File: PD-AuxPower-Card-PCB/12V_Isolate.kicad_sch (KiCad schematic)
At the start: 32 parts, among them J4 2.54mm terminal, Q1 FDMC86520L, T1 ER 9.5, U12 TL431DBZ, U7 LTV-217

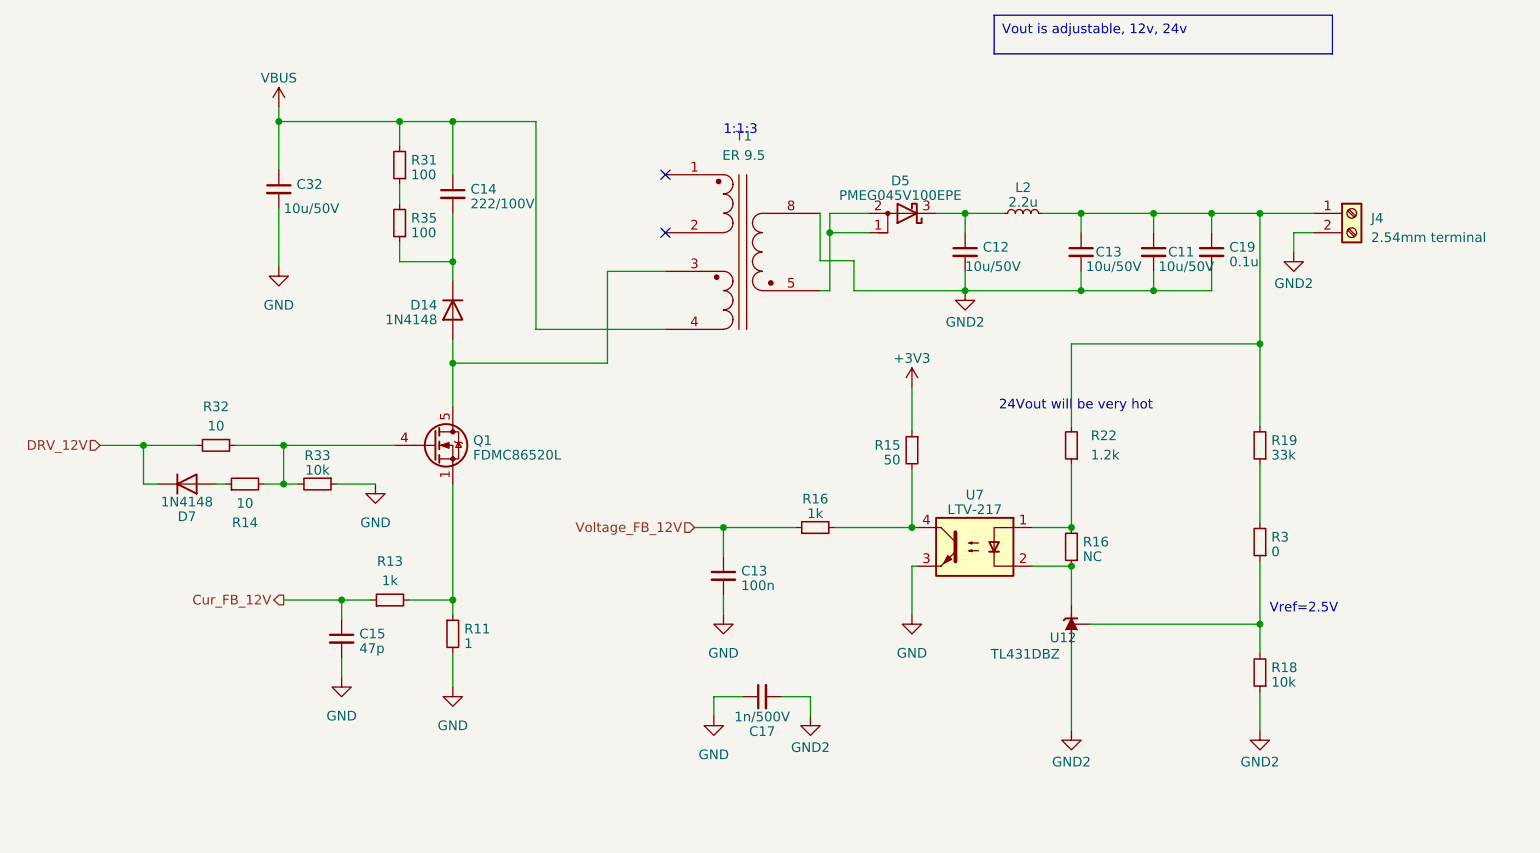
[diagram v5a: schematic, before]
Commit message: FEAT: Set I2C mode to standard mode(100kHz), change FUSB302B driver header file definition, trimming output voltage of 3.3/5V channel and 12/24V channel by optocoupler current reduce to 1mA. Add reserved PD protocol header and source file named pd_sink.h/.c. Add FUSB302B initial sequence and read/write driver. PCB: remove some unused protection diode, modify resistance.
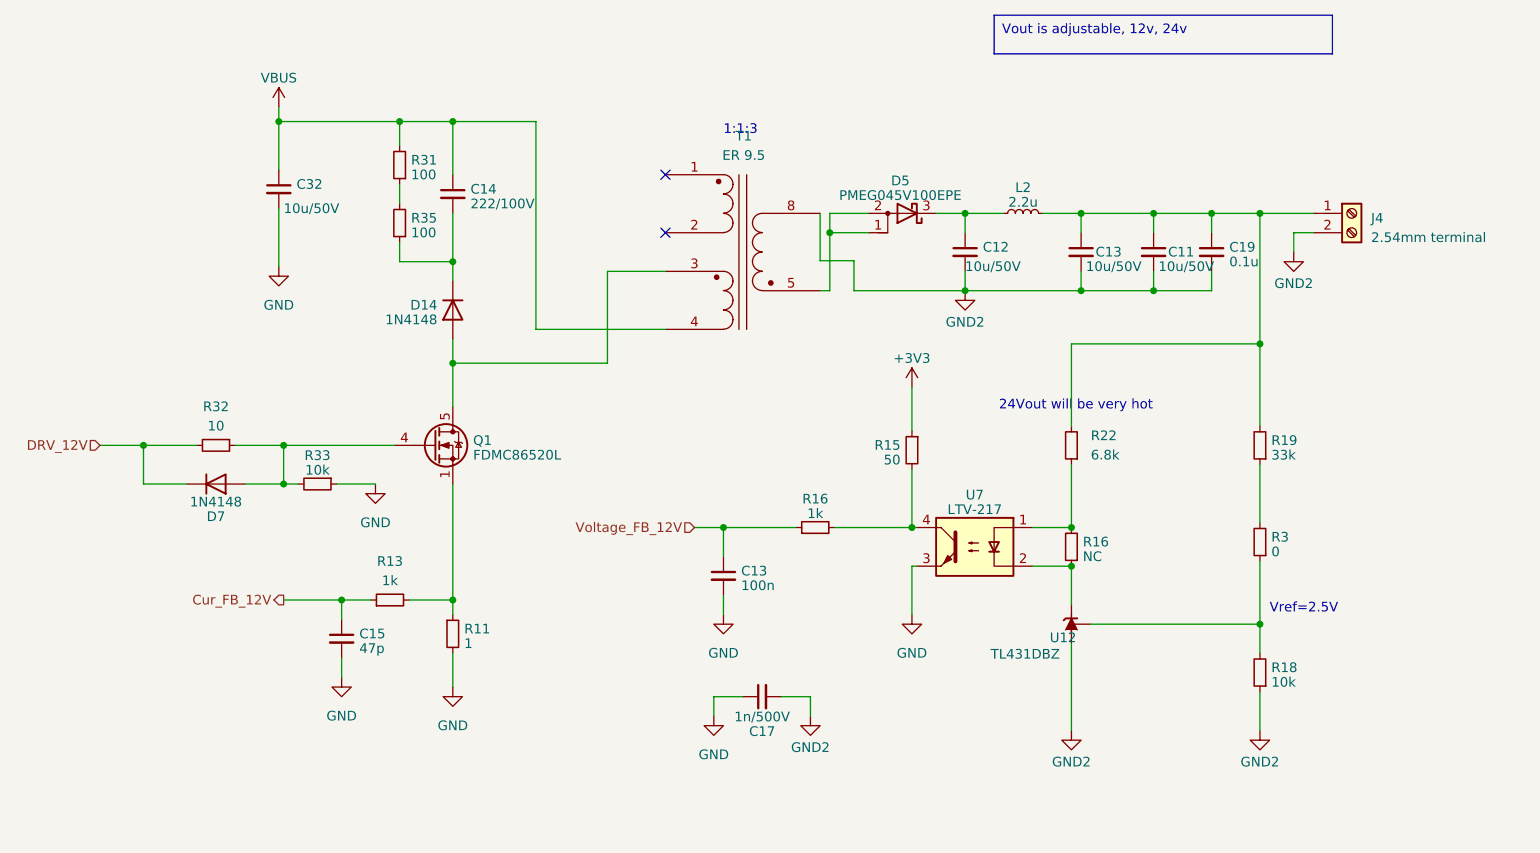
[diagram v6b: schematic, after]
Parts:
- removed R14: 10, Resistor_SMD:R_0402_1005Metric, symbol Device:R_Small
- R22: value 1.2k -> 6.8k
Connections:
- net at Q1.4 (G), R32.1, R33.2: now also D7.2 (A)
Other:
- moved on the sheet: D7
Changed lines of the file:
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@@
     (stroke (width 0) (type default))
   )
-  (wire (pts (xy 93.345 96.52) (xy 95.885 96.52))
+  (wire (pts (xy 90.805 96.52) (xy 95.885 96.52))
     (stroke (width 0) (type default))
   )
@@
     (stroke (width 0) (type default))
   )
-  (wire (pts (xy 77.47 96.52) (xy 79.375 96.52))
+  (wire (pts (xy 77.47 96.52) (xy 83.185 96.52))
     (stroke (width 0) (type default))
   )
@@
   )
   (wire (pts (xy 111.125 48.895) (xy 118.11 48.895))
-    (stroke (width 0) (type default))
-  )
-  (wire (pts (xy 86.995 96.52) (xy 88.265 96.52))
     (stroke (width 0) (type default))
   )
@@
     )
   )
-  (symbol (lib_id "Diode:1N4148") (at 83.185 96.52 0) (mirror x) (unit 1)
+  (symbol (lib_id "Diode:1N4148") (at 86.995 96.52 0) (mirror x) (unit 1)
     (in_bom yes) (on_board yes) (dnp no)
-    (property "Reference" "D7" (at 83.185 100.7999 0)
-      (effects (font (size 1.27 1.27)))
-    )
-    (property "Value" "1N4148" (at 83.185 98.8789 0)
-      (effects (font (size 1.27 1.27)))
-    )
-    (property "Footprint" "Diode_SMD:D_SOD-523" (at 83.185 96.52 0)
-      (effects (font (size 1.27 1.27)) hide)
-    )
-    (property "Datasheet" "https://assets.nexperia.com/documents/data-sheet/1N4148_1N4448.pdf" (at 83.185 96.52 0)
-      (effects (font (size 1.27 1.27)) hide)
-    )
-    (property "Sim.Device" "D" (at 83.185 96.52 0)
-      (effects (font (size 1.27 1.27)) hide)
-    )
-    (property "Sim.Pins" "1=K 2=A" (at 83.185 96.52 0)
+    (property "Reference" "D7" (at 86.995 100.7999 0)
+      (effects (font (size 1.27 1.27)))
+    )
+    (property "Value" "1N4148" (at 86.995 98.8789 0)
+      (effects (font (size 1.27 1.27)))
+    )
+    (property "Footprint" "Diode_SMD:D_SOD-523" (at 86.995 96.52 0)
+      (effects (font (size 1.27 1.27)) hide)
+    )
+    (property "Datasheet" "https://assets.nexperia.com/documents/data-sheet/1N4148_1N4448.pdf" (at 86.995 96.52 0)
+      (effects (font (size 1.27 1.27)) hide)
+    )
+    (property "Sim.Device" "D" (at 86.995 96.52 0)
+      (effects (font (size 1.27 1.27)) hide)
+    )
+    (property "Sim.Pins" "1=K 2=A" (at 86.995 96.52 0)
       (effects (font (size 1.27 1.27)) hide)
     )
@@
       (effects (font (size 1.27 1.27)) (justify right))
     )
-    (property "Value" "1.2k" (at 201.93 92.71 0)
+    (property "Value" "6.8k" (at 201.93 92.71 0)
       (effects (font (size 1.27 1.27)) (justify right))
     )
@@
         )
       )
-    )
-  )
-  (symbol (lib_id "Device:R_Small") (at 90.805 96.52 90) (unit 1)
-    (in_bom yes) (on_board yes) (dnp no)
-    (property "Reference" "R14" (at 90.805 101.6 90)
-      (effects (font (size 1.27 1.27)))
-    )
-    (property "Value" "10" (at 90.805 99.06 90)
-      (effects (font (size 1.27 1.27)))
-    )
-    (property "Footprint" "Resistor_SMD:R_0402_1005Metric" (at 90.805 96.52 0)
-      (effects (font (size 1.27 1.27)) hide)
-    )
-    (property "Datasheet" "~" (at 90.805 96.52 0)
-      (effects (font (size 1.27 1.27)) hide)
-    )
-    (pin "1")
-    (pin "2")
-    (instances
-      (project "PD-AuxPower-Card"
-        (path "/48c5bc14-ccc3-44de-b526-838e3d53c0ee/40f113c1-6183-4863-b2ec-a4ca33698158"
-          (reference "R14") (unit 1)
-        )
-        (path "/48c5bc14-ccc3-44de-b526-838e3d53c0ee/9a44a331-fce1-4dee-b5a9-6d547d8c4b08"
-          (reference "R47") (unit 1)
-        )
-      )

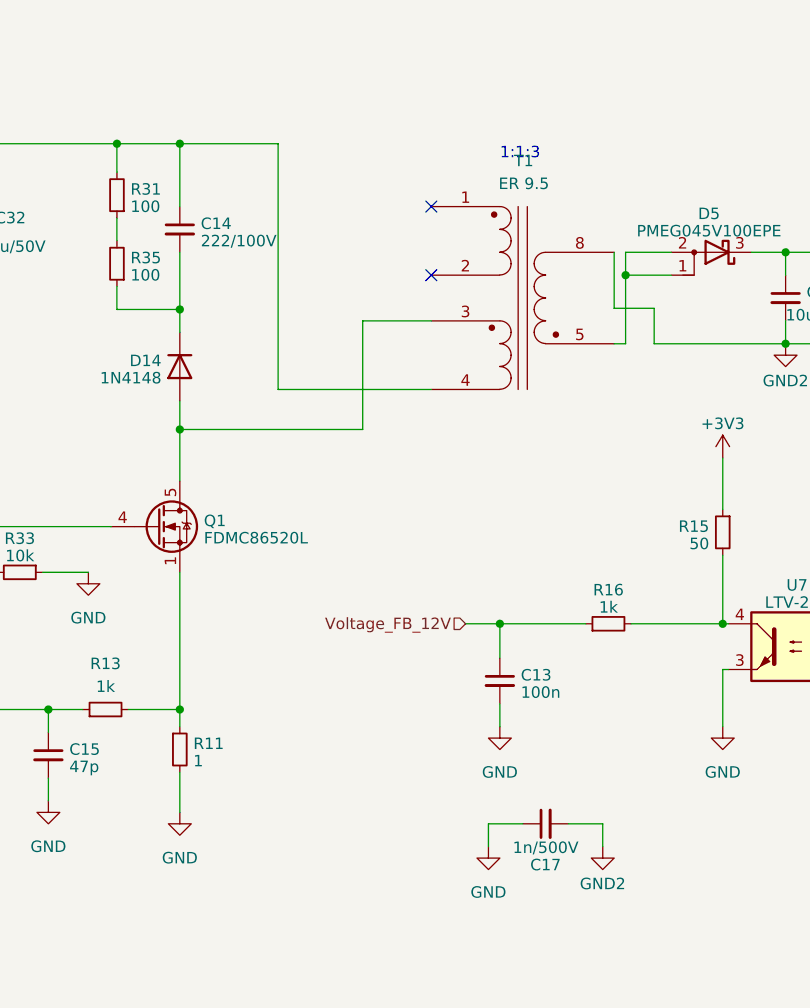
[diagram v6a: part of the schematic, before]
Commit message: FEAT: Revolution PCB to ver 1.0. Change COMP1+ to 3v3 current sense, COMP2+ to 12V current sense and 12V LED to GPIO7 output. Modify PCB layout.
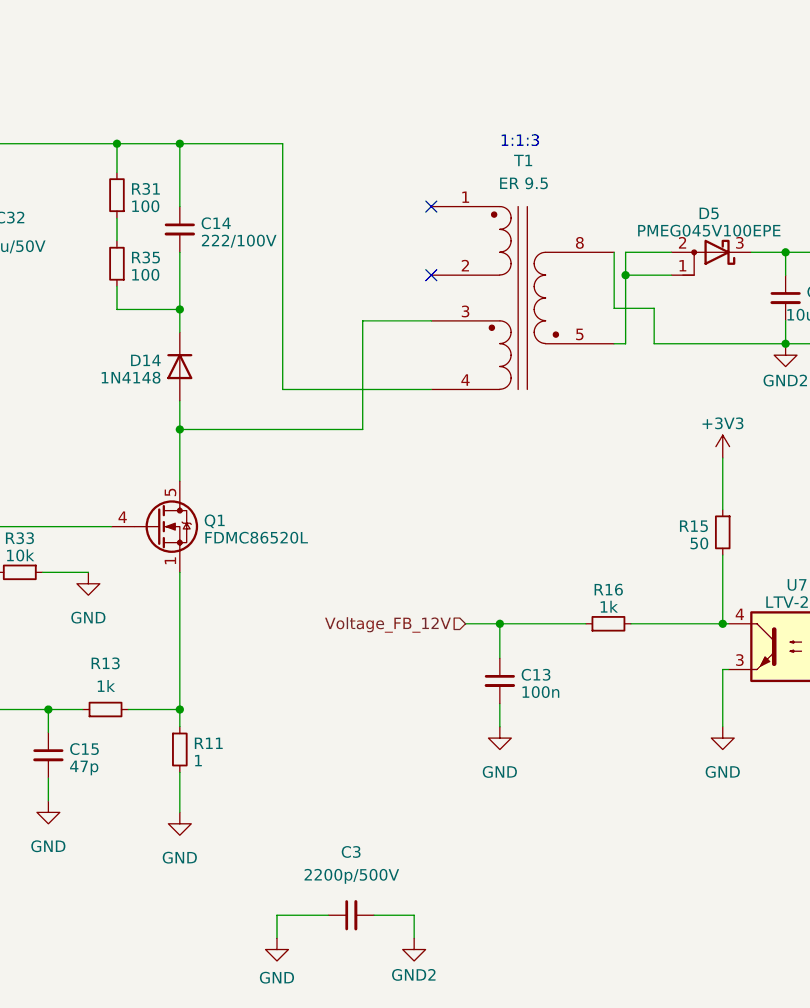
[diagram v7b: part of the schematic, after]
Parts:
- removed C17: 1n/500V, Capacitor_SMD:C_1210_3225Metric, symbol Device:C_Small
- added C3: 2200p/500V, Capacitor_SMD:C_1206_3216Metric, symbol Device:C_Small
- T1: footprint User:Transformer_ER9.5_11.6mmx8.2mm -> Johnson's:Transformer_ER9.5_11.6mmx8.2mm
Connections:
- net GND: now also C3.1
- net GND2: now also C3.2
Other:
- company: (none) -> Habonroof Playground
- title: (none) -> 12/24V Flyback converter
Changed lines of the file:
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@@
 (kicad_sch (version 20230121) (generator eeschema)
   (paper "A4")
+  (title_block
+    (title "12/24V Flyback converter")
+    (date "2023-11-26")
+    (rev "Rev 1.0")
+    (company "Habonroof Playground")
+  )
   (junction (at 95.885 91.44) (diameter 0) (color 0 0 0 0)
   )
@@
     (stroke (width 0) (type default))
   )
-  (wire (pts (xy 156.21 124.46) (xy 152.4 124.46))
-    (stroke (width 0) (type default))
-  )
   (wire (pts (xy 200.66 68.58) (xy 200.66 71.12))
     (stroke (width 0) (type default))
@@
     (stroke (width 0) (type default))
   )
-  (wire (pts (xy 146.05 76.2) (xy 129.032 76.2))
+  (wire (pts (xy 146.05 76.2) (xy 129.54 76.2))
     (stroke (width 0) (type default))
   )
@@
     (stroke (width 0) (type default))
   )
+  (wire (pts (xy 144.145 134.62) (xy 144.145 137.16))
+    (stroke (width 0) (type default))
+  )
   (wire (pts (xy 168.275 102.235) (xy 178.435 102.235))
     (stroke (width 0) (type default))
@@
     (stroke (width 0) (type default))
   )
-  (wire (pts (xy 129.032 76.2) (xy 129.032 48.895))
+  (wire (pts (xy 129.54 76.2) (xy 129.54 48.895))
     (stroke (width 0) (type default))
   )
@@
     (stroke (width 0) (type default))
   )
-  (wire (pts (xy 161.29 124.46) (xy 165.1 124.46))
-    (stroke (width 0) (type default))
-  )
   (wire (pts (xy 178.435 94.615) (xy 178.435 102.235))
     (stroke (width 0) (type default))
   )
-  (wire (pts (xy 118.11 48.895) (xy 129.032 48.895))
-    (stroke (width 0) (type default))
-  )
-  (wire (pts (xy 165.1 124.46) (xy 165.1 127))
+  (wire (pts (xy 118.11 48.895) (xy 129.54 48.895))
+    (stroke (width 0) (type default))
+  )
+  (wire (pts (xy 128.905 134.62) (xy 134.62 134.62))
     (stroke (width 0) (type default))
   )
@@
     (stroke (width 0) (type default))
   )
+  (wire (pts (xy 128.905 137.16) (xy 128.905 134.62))
+    (stroke (width 0) (type default))
+  )
   (wire (pts (xy 118.11 67.31) (xy 118.11 69.85))
     (stroke (width 0) (type default))
@@
     (stroke (width 0) (type default))
   )
-  (wire (pts (xy 152.4 124.46) (xy 152.4 127))
-    (stroke (width 0) (type default))
-  )
   (wire (pts (xy 107.315 111.76) (xy 103.505 111.76))
     (stroke (width 0) (type default))
@@
   )
   (wire (pts (xy 118.11 80.645) (xy 118.11 86.36))
+    (stroke (width 0) (type default))
+  )
+  (wire (pts (xy 139.7 134.62) (xy 144.145 134.62))
     (stroke (width 0) (type default))
   )
@@
     (effects (font (size 1.27 1.27)) (justify left bottom))
   )
-  (text "1:1:3" (at 153.67 50.8 0)
+  (text "1:1:3" (at 153.67 49.53 0)
     (effects (font (size 1.27 1.27)) (justify left bottom))
   )
@@
         (path "/48c5bc14-ccc3-44de-b526-838e3d53c0ee/9a44a331-fce1-4dee-b5a9-6d547d8c4b08"
           (reference "D18") (unit 1)
-        )
-      )
-    )
-  )
-  (symbol (lib_id "power:GND") (at 152.4 127 0) (unit 1)
-    (in_bom yes) (on_board yes) (dnp no) (fields_autoplaced)
-    (property "Reference" "#PWR08" (at 152.4 133.35 0)
-      (effects (font (size 1.27 1.27)) hide)
-    )
-    (property "Value" "GND" (at 152.4 132.08 0)
-      (effects (font (size 1.27 1.27)))
-    )
-    (property "Footprint" "" (at 152.4 127 0)
-      (effects (font (size 1.27 1.27)) hide)
-    )
-    (property "Datasheet" "" (at 152.4 127 0)
-      (effects (font (size 1.27 1.27)) hide)
-    )
-    (pin "1")
-    (instances
-      (project "PD-AuxPower-Card"
-        (path "/48c5bc14-ccc3-44de-b526-838e3d53c0ee"
-          (reference "#PWR08") (unit 1)
-        )
-        (path "/48c5bc14-ccc3-44de-b526-838e3d53c0ee/40f113c1-6183-4863-b2ec-a4ca33698158"
-          (reference "#PWR051") (unit 1)
-        )
-        (path "/48c5bc14-ccc3-44de-b526-838e3d53c0ee/9a44a331-fce1-4dee-b5a9-6d547d8c4b08"
-          (reference "#PWR085") (unit 1)
         )
       )
@@
     )
   )
-  (symbol (lib_id "Device:C_Small") (at 158.75 124.46 90) (mirror x) (unit 1)
+  (symbol (lib_id "power:GND") (at 128.905 137.16 0) (unit 1)
     (in_bom yes) (on_board yes) (dnp no)
-    (property "Reference" "C17" (at 158.7563 129.032 90)
-      (effects (font (size 1.27 1.27)))
-    )
-    (property "Value" "1n/500V" (at 158.7563 127.111 90)
-      (effects (font (size 1.27 1.27)))
-    )
-    (property "Footprint" "Capacitor_SMD:C_1210_3225Metric" (at 158.75 124.46 0)
-      (effects (font (size 1.27 1.27)) hide)
-    )
-    (property "Datasheet" "~" (at 158.75 124.46 0)
-      (effects (font (size 1.27 1.27)) hide)
-    )
-    (pin "1")
-    (pin "2")
-    (instances
-      (project "PD-AuxPower-Card"
-        (path "/48c5bc14-ccc3-44de-b526-838e3d53c0ee/40f113c1-6183-4863-b2ec-a4ca33698158"
-          (reference "C17") (unit 1)
-        )
-        (path "/48c5bc14-ccc3-44de-b526-838e3d53c0ee/9a44a331-fce1-4dee-b5a9-6d547d8c4b08"
-          (reference "C36") (unit 1)
+    (property "Reference" "#PWR08" (at 128.905 143.51 0)
+      (effects (font (size 1.27 1.27)) hide)
+    )
+    (property "Value" "GND" (at 128.905 141.605 0)
+      (effects (font (size 1.27 1.27)))
+    )
+    (property "Footprint" "" (at 128.905 137.16 0)
+      (effects (font (size 1.27 1.27)) hide)
+    )
+    (property "Datasheet" "" (at 128.905 137.16 0)
+      (effects (font (size 1.27 1.27)) hide)
+    )
+    (pin "1")
+    (instances
+      (project "PD-AuxPower-Card"
+        (path "/48c5bc14-ccc3-44de-b526-838e3d53c0ee"
+          (reference "#PWR08") (unit 1)
+        )
+        (path "/48c5bc14-ccc3-44de-b526-838e3d53c0ee/40f113c1-6183-4863-b2ec-a4ca33698158"
+          (reference "#PWR04") (unit 1)
+        )
+        (path "/48c5bc14-ccc3-44de-b526-838e3d53c0ee/9a44a331-fce1-4dee-b5a9-6d547d8c4b08"
+          (reference "#PWR033") (unit 1)
         )
       )
@@
       (effects (font (size 1.27 1.27)))
     )
-    (property "Footprint" "User:Transformer_ER9.5_11.6mmx8.2mm" (at 156.21 66.04 0)
+    (property "Footprint" "Johnson's:Transformer_ER9.5_11.6mmx8.2mm" (at 156.21 66.04 0)
       (effects (font (size 1.27 1.27)) hide)
     )
@@
     )
   )
+  (symbol (lib_id "power:GND2") (at 144.145 137.16 0) (unit 1)
+    (in_bom yes) (on_board yes) (dnp no) (fields_autoplaced)
+    (property "Reference" "#PWR034" (at 144.145 143.51 0)
+      (effects (font (size 1.27 1.27)) hide)
+    )
+    (property "Value" "GND2" (at 144.145 141.2955 0)
+      (effects (font (size 1.27 1.27)))
+    )
+    (property "Footprint" "" (at 144.145 137.16 0)
+      (effects (font (size 1.27 1.27)) hide)
+    )
+    (property "Datasheet" "" (at 144.145 137.16 0)
+      (effects (font (size 1.27 1.27)) hide)
+    )
+    (pin "1")
+    (instances
+      (project "PD-AuxPower-Card"
+        (path "/48c5bc14-ccc3-44de-b526-838e3d53c0ee/9a44a331-fce1-4dee-b5a9-6d547d8c4b08"
+          (reference "#PWR034") (unit 1)
+        )
+      )
+    )
+  )
   (symbol (lib_id "Device:R_Small") (at 165.735 102.235 90) (unit 1)
     (in_bom yes) (on_board yes) (dnp no) (fields_autoplaced)
@@
         (path "/48c5bc14-ccc3-44de-b526-838e3d53c0ee/9a44a331-fce1-4dee-b5a9-6d547d8c4b08"
           (reference "R17") (unit 1)
+        )
+      )
+    )
+  )
+  (symbol (lib_id "Device:C_Small") (at 137.16 134.62 90) (unit 1)
+    (in_bom yes) (on_board yes) (dnp no) (fields_autoplaced)
+    (property "Reference" "C3" (at 137.1663 127.635 90)
+      (effects (font (size 1.27 1.27)))
+    )
+    (property "Value" "2200p/500V" (at 137.1663 130.175 90)
+      (effects (font (size 1.27 1.27)))
+    )
+    (property "Footprint" "Capacitor_SMD:C_1206_3216Metric" (at 137.16 134.62 0)
+      (effects (font (size 1.27 1.27)) hide)
+    )
+    (property "Datasheet" "~" (at 137.16 134.62 0)
+      (effects (font (size 1.27 1.27)) hide)
+    )
+    (pin "1")
+    (pin "2")
+    (instances
+      (project "PD-AuxPower-Card"
+        (path "/48c5bc14-ccc3-44de-b526-838e3d53c0ee/40f113c1-6183-4863-b2ec-a4ca33698158"
+          (reference "C3") (unit 1)
+        )
+        (path "/48c5bc14-ccc3-44de-b526-838e3d53c0ee/9a44a331-fce1-4dee-b5a9-6d547d8c4b08"
+          (reference "C5") (unit 1)
         )
       )
@@
         )
       )
-    )
-  )
-  (symbol (lib_id "power:GND2") (at 165.1 127 0) (unit 1)
-    (in_bom yes) (on_board yes) (dnp no) (fields_autoplaced)
-    (property "Reference" "#PWR086" (at 165.1 133.35 0)
-      (effects (font (size 1.27 1.27)) hide)
-    )
-    (property "Value" "GND2" (at 165.1 131.1355 0)
-      (effects (font (size 1.27 1.27)))
-    )
-    (property "Footprint" "" (at 165.1 127 0)
-      (effects (font (size 1.27 1.27)) hide)
-    )
-    (property "Datasheet" "" (at 165.1 127 0)
-      (effects (font (size 1.27 1.27)) hide)
-    )
-    (pin "1")
-    (instances
-      (project "PD-AuxPower-Card"
-        (path "/48c5bc14-ccc3-44de-b526-838e3d53c0ee/9a44a331-fce1-4dee-b5a9-6d547d8c4b08"
-          (reference "#PWR086") (unit 1)
-        )
-      )
